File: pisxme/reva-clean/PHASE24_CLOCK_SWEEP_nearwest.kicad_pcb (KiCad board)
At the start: 6 copper layers, 300 x 180 mm, 94 parts, among them J1 74221-101LF, J2 A70-112-331N126, J3 JAE SM3ZS067U410ABR1000 B-key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, J4 Amphenol 10171746-00021LF USB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, J5 0039300020, J6 0039300020, J7 Raspberry-Pi-5-Compute-Module, Q1 CSD19536KCS, Q2 CSD19536KCS, U1 LM74700QDBVRQ1, U2 LM74700QDBVRQ1, U3 TPSM63606RDLR, U4 TPSM63606RDLR, U5 TPSM63606RDLR, U6 TPD4EUSB30, U7 TUSB9261IPVP, U8 Texas_DRT_3, U9 TPD4EUSB30

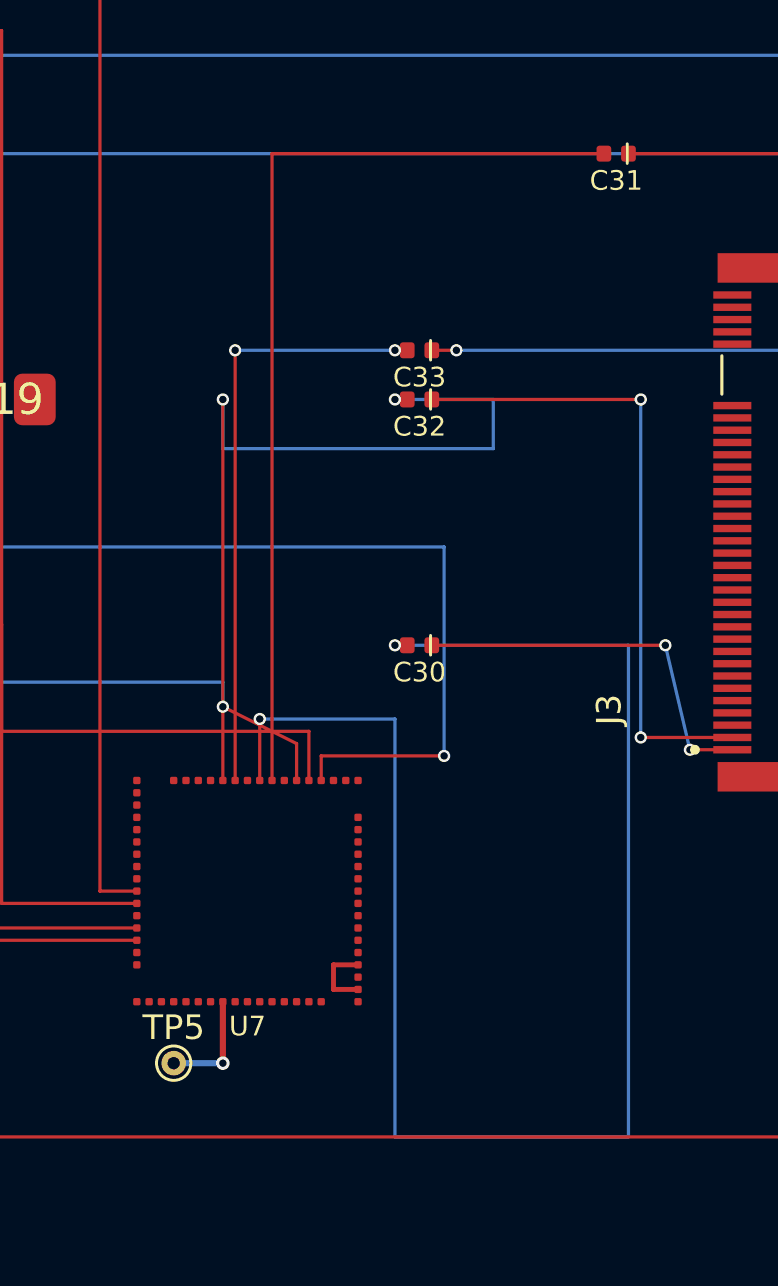
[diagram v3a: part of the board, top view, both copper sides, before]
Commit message: phase24 reject sata launch dogleg
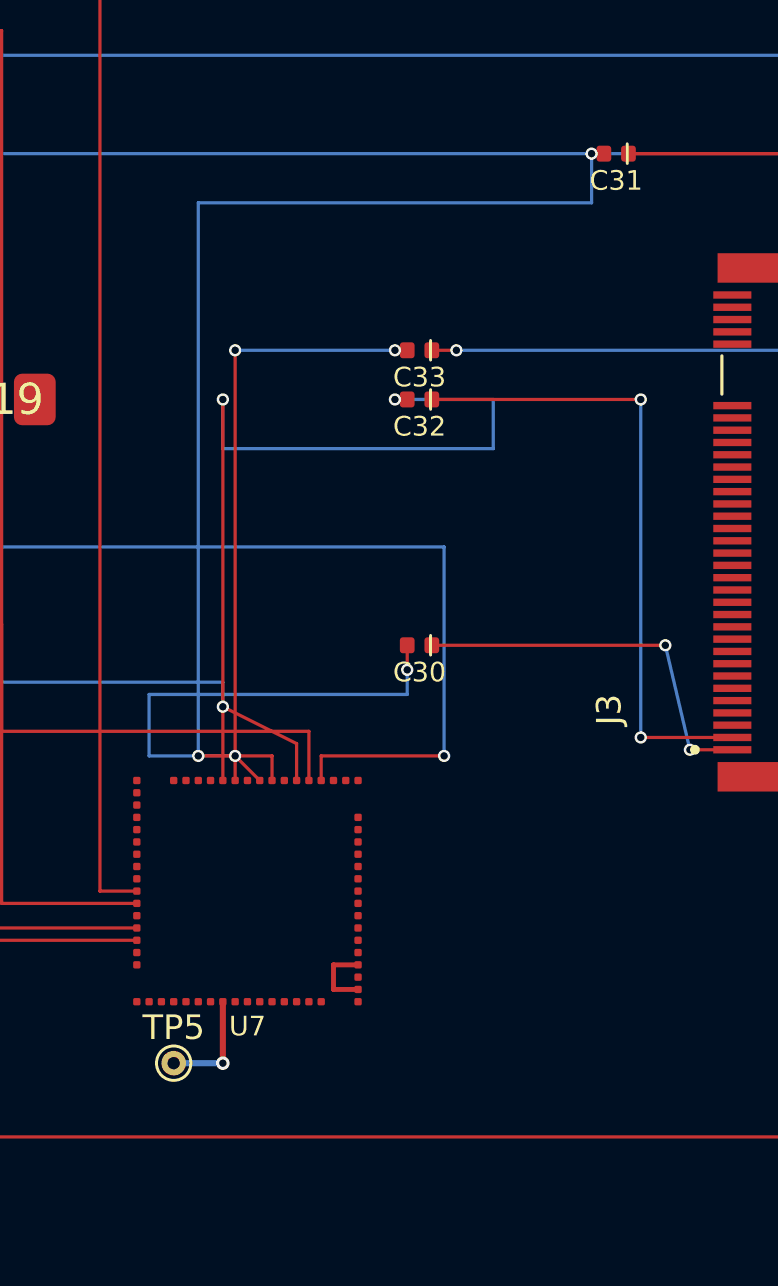
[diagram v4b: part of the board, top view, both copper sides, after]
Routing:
- net /STORAGE/BRIDGE_SATA_TX_P: track 64.5 -> 19.9 mm
- net /STORAGE/BRIDGE_SATA_TX_N: track 39.0 -> 45.0 mm, vias 0 -> 2
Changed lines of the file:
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@@
 		(embedded_fonts no)
 	)
-	(footprint "Crystal_3225_4Pad"
-		(layer "F.Cu")
-		(at 108 130)
-		(descr "3.2 x 2.5 mm 4-pad crystal; verify vendor pad numbering before release")
-		(property "Reference" "Y1"
-			(at 0 0 0)
-			(layer "F.SilkS")
-			(effects
-				(font
-					(size 1.27 1.27)
-				)
-			)
-		)
-		(property "Value" ""
-			(at 0 0 0)
-			(layer "F.Fab")
-			(effects
-				(font
-					(size 1.27 1.27)
-				)
-			)
-		)
-		(property "Datasheet" ""
-			(at 0 0 0)
-			(layer "F.Fab")
-			(hide yes)
-			(effects
-				(font
-					(size 1.27 1.27)
-				)
-			)
-		)
-		(property "Description" ""
-			(at 0 0 0)
-			(layer "F.Fab")
-			(hide yes)
-			(effects
-				(font
-					(size 1.27 1.27)
-				)
-			)
-		)
-		(duplicate_pad_numbers_are_jumpers no)
-		(fp_rect
-			(start -1.6 -1.25)
-			(end 1.6 1.25)
-			(stroke
-				(width 0.12)
-				(type default)
-			)
-			(fill no)
-			(layer "F.SilkS")
-		)
-		(fp_rect
-			(start -1.7 -1.35)
-			(end 1.7 1.35)
-			(stroke
-				(width 0.05)
-				(type default)
-			)
-			(fill no)
-			(layer "F.CrtYd")
-		)
-		(pad "1" smd roundrect
-			(at -1.1 -0.85)
-			(size 1.2 0.9)
-			(layers "F.Cu" "F.Mask" "F.Paste")
-			(roundrect_rratio 0.2)
-			(net "/STORAGE/BRIDGE_XI")
-		)
-		(pad "2" smd roundrect
-			(at -1.1 0.85)
-			(size 1.2 0.9)
-			(layers "F.Cu" "F.Mask" "F.Paste")
-			(roundrect_rratio 0.2)
-			(net "/STORAGE/BRIDGE_VSSOSC")
-		)
-		(pad "3" smd roundrect
-			(at 1.1 0.85)
-			(size 1.2 0.9)
-			(layers "F.Cu" "F.Mask" "F.Paste")
-			(roundrect_rratio 0.2)
-			(net "/STORAGE/BRIDGE_XO")
-		)
-		(pad "4" smd roundrect
-			(at 1.1 -0.85)
-			(size 1.2 0.9)
-			(layers "F.Cu" "F.Mask" "F.Paste")
-			(roundrect_rratio 0.2)
-			(net "/STORAGE/BRIDGE_VSSOSC")
-		)
-		(embedded_fonts no)
-	)
 	(footprint "TVS_SMBJ18A_DO214AA"
 		(layer "F.Cu")
@@
 		(embedded_fonts no)
 	)
+	(footprint "Crystal_3225_4Pad"
+		(layer "F.Cu")
+		(at 108 130)
+		(descr "3.2 x 2.5 mm 4-pad crystal; verify vendor pad numbering before release")
+		(property "Reference" "Y1"
+			(at 0 0 0)
+			(layer "F.SilkS")
+			(effects
+				(font
+					(size 1.27 1.27)
+				)
+			)
+		)
+		(property "Value" ""
+			(at 0 0 0)
+			(layer "F.Fab")
+			(effects
+				(font
+					(size 1.27 1.27)
+				)
+			)
+		)
+		(property "Datasheet" ""
+			(at 0 0 0)
+			(layer "F.Fab")
+			(hide yes)
+			(effects
+				(font
+					(size 1.27 1.27)
+				)
+			)
+		)
+		(property "Description" ""
+			(at 0 0 0)
+			(layer "F.Fab")
+			(hide yes)
+			(effects
+				(font
+					(size 1.27 1.27)
+				)
+			)
+		)
+		(duplicate_pad_numbers_are_jumpers no)
+		(fp_rect
+			(start -1.6 -1.25)
+			(end 1.6 1.25)
+			(stroke
+				(width 0.12)
+				(type default)
+			)
+			(fill no)
+			(layer "F.SilkS")
+		)
+		(fp_rect
+			(start -1.7 -1.35)
+			(end 1.7 1.35)
+			(stroke
+				(width 0.05)
+				(type default)
+			)
+			(fill no)
+			(layer "F.CrtYd")
+		)
+		(pad "1" smd roundrect
+			(at -1.1 -0.85)
+			(size 1.2 0.9)
+			(layers "F.Cu" "F.Mask" "F.Paste")
+			(roundrect_rratio 0.2)
+			(net "/STORAGE/BRIDGE_XI")
+		)
+		(pad "2" smd roundrect
+			(at -1.1 0.85)
+			(size 1.2 0.9)
+			(layers "F.Cu" "F.Mask" "F.Paste")
+			(roundrect_rratio 0.2)
+			(net "/STORAGE/BRIDGE_VSSOSC")
+		)
+		(pad "3" smd roundrect
+			(at 1.1 0.85)
+			(size 1.2 0.9)
+			(layers "F.Cu" "F.Mask" "F.Paste")
+			(roundrect_rratio 0.2)
+			(net "/STORAGE/BRIDGE_XO")
+		)
+		(pad "4" smd roundrect
+			(at 1.1 -0.85)
+			(size 1.2 0.9)
+			(layers "F.Cu" "F.Mask" "F.Paste")
+			(roundrect_rratio 0.2)
+			(net "/STORAGE/BRIDGE_VSSOSC")
+		)
+		(embedded_fonts no)
+	)
 	(footprint "R_0402_1005Metric"
 		(layer "F.Cu")
@@
 	)
 	(segment
-		(start 121 110)
-		(end 134.5 110)
-		(width 0.13208)
+		(start 121 134.5)
+		(end 118 134.5)
+		(width 0.1321)
 		(layer "F.Cu")
 		(net "/STORAGE/BRIDGE_SATA_TX_N")
@@
 	(segment
 		(start 121 135.5)
-		(end 121 110)
-		(width 0.13208)
+		(end 121 134.5)
+		(width 0.1321)
 		(layer "F.Cu")
 		(net "/STORAGE/BRIDGE_SATA_TX_N")
 	)
 	(segment
-		(start 126 130)
+		(start 134 110)
+		(end 134.5 110)
+		(width 0.1321)
+		(layer "F.Cu")
+		(net "/STORAGE/BRIDGE_SATA_TX_N")
+	)
+	(via
+		(at 134 110)
+		(size 0.5)
+		(drill 0.3)
+		(layers "F.Cu" "B.Cu")
+		(net "/STORAGE/BRIDGE_SATA_TX_N")
+	)
+	(via
+		(at 118 134.5)
+		(size 0.5)
+		(drill 0.3)
+		(layers "F.Cu" "B.Cu")
+		(net "/STORAGE/BRIDGE_SATA_TX_N")
+	)
+	(segment
+		(start 118 134.5)
+		(end 118 112)
+		(width 0.1321)
+		(layer "B.Cu")
+		(net "/STORAGE/BRIDGE_SATA_TX_N")
+	)
+	(segment
+		(start 118 112)
+		(end 134 112)
+		(width 0.1321)
+		(layer "B.Cu")
+		(net "/STORAGE/BRIDGE_SATA_TX_N")
+	)
+	(segment
+		(start 134 112)
+		(end 134 110)
+		(width 0.1321)
+		(layer "B.Cu")
+		(net "/STORAGE/BRIDGE_SATA_TX_N")
+	)
+	(segment
+		(start 126.5 131)
 		(end 126.5 130)
-		(width 0.13208)
+		(width 0.1321)
 		(layer "F.Cu")
 		(net "/STORAGE/BRIDGE_SATA_TX_P")
@@
 	(segment
 		(start 120.5 135.5)
-		(end 120.5 133)
-		(width 0.13208)
+		(end 119.5 134.5)
+		(width 0.1321)
 		(layer "F.Cu")
 		(net "/STORAGE/BRIDGE_SATA_TX_P")
 	)
 	(via
-		(at 120.5 133)
+		(at 119.5 134.5)
 		(size 0.5)
 		(drill 0.3)
@@
 	)
 	(via
-		(at 126 130)
+		(at 126.5 131)
 		(size 0.5)
 		(drill 0.3)
@@
 	)
 	(segment
-		(start 126 150)
-		(end 135.5 150)
-		(width 0.13208)
-		(layer "B.Cu")
-		(net "/STORAGE/BRIDGE_SATA_TX_P")
-	)
-	(segment
-		(start 135.5 130)
-		(end 126 130)
-		(width 0.13208)
+		(start 126.5 132)
+		(end 126.5 131)
+		(width 0.1321)
 		(layer "B.Cu")
 		(net "/STORAGE/BRIDGE_SATA_TX_P")
 	)
 	(segment
-		(start 135.5 150)
-		(end 135.5 130)
-		(width 0.13208)
+		(start 116 134.5)
+		(end 116 132)
+		(width 0.1321)
 		(layer "B.Cu")
 		(net "/STORAGE/BRIDGE_SATA_TX_P")
 	)
 	(segment
-		(start 126 133)
-		(end 126 150)
-		(width 0.13208)
+		(start 119.5 134.5)
+		(end 116 134.5)
+		(width 0.1321)
 		(layer "B.Cu")
 		(net "/STORAGE/BRIDGE_SATA_TX_P")
 	)
 	(segment
-		(start 120.5 133)
-		(end 126 133)
-		(width 0.13208)
+		(start 116 132)
+		(end 126.5 132)
+		(width 0.1321)
 		(layer "B.Cu")
 		(net "/STORAGE/BRIDGE_SATA_TX_P")
@@
 	)
 	(segment
-		(start 123 134.5)
-		(end 128 134.5)
+		(start 123 135.5)
+		(end 123 134.5)
 		(width 0.1321)
 		(layer "F.Cu")
@@
 	)
 	(segment
-		(start 123 135.5)
-		(end 123 134.5)
+		(start 123 134.5)
+		(end 128 134.5)
 		(width 0.1321)
 		(layer "F.Cu")
@@
 	)
 	(segment
-		(start 106.9 126)
-		(end 106.9 129.15)
+		(start 128 126)
+		(end 106.9 126)
 		(width 0.1321)
 		(layer "B.Cu")
@@
 	)
 	(segment
-		(start 128 126)
-		(end 106.9 126)
+		(start 128 134.5)
+		(end 128 126)
 		(width 0.1321)
 		(layer "B.Cu")
@@
 	)
 	(segment
-		(start 128 134.5)
-		(end 128 126)
+		(start 106.9 126)
+		(end 106.9 129.15)
 		(width 0.1321)
 		(layer "B.Cu")
@@
 	)
 	(segment
-		(start 110 129.15)
-		(end 109.1 129.15)
+		(start 122.5 135.5)
+		(end 122.5 133.5)
 		(width 0.1321)
 		(layer "F.Cu")
@@
 	)
 	(segment
-		(start 122.5 135.5)
-		(end 122.5 133.5)
+		(start 122.5 133.5)
+		(end 110 133.5)
 		(width 0.1321)
 		(layer "F.Cu")
@@
 	)
 	(segment
-		(start 110 133.5)
-		(end 110 129.15)
+		(start 110 129.15)
+		(end 109.1 129.15)
 		(width 0.1321)
 		(layer "F.Cu")
@@
 	)
 	(segment
-		(start 122.5 133.5)
-		(end 110 133.5)
+		(start 110 133.5)
+		(end 110 129.15)
 		(width 0.1321)
 		(layer "F.Cu")
